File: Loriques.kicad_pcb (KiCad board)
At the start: 4 copper layers, 144.8 x 106.7 mm, 130 parts, among them IC10 MAX17263LETD+T, IC12 TPS22975, IC14 W25Q64FWSSIG, IC19 TPS22975, IC2 MCP73871, IC3 HDC2080, IC4 TPS2013A, IC5 CAT25160VI-GT3, IC6 SN74LVC244A, IC7 LP38691-ADJ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

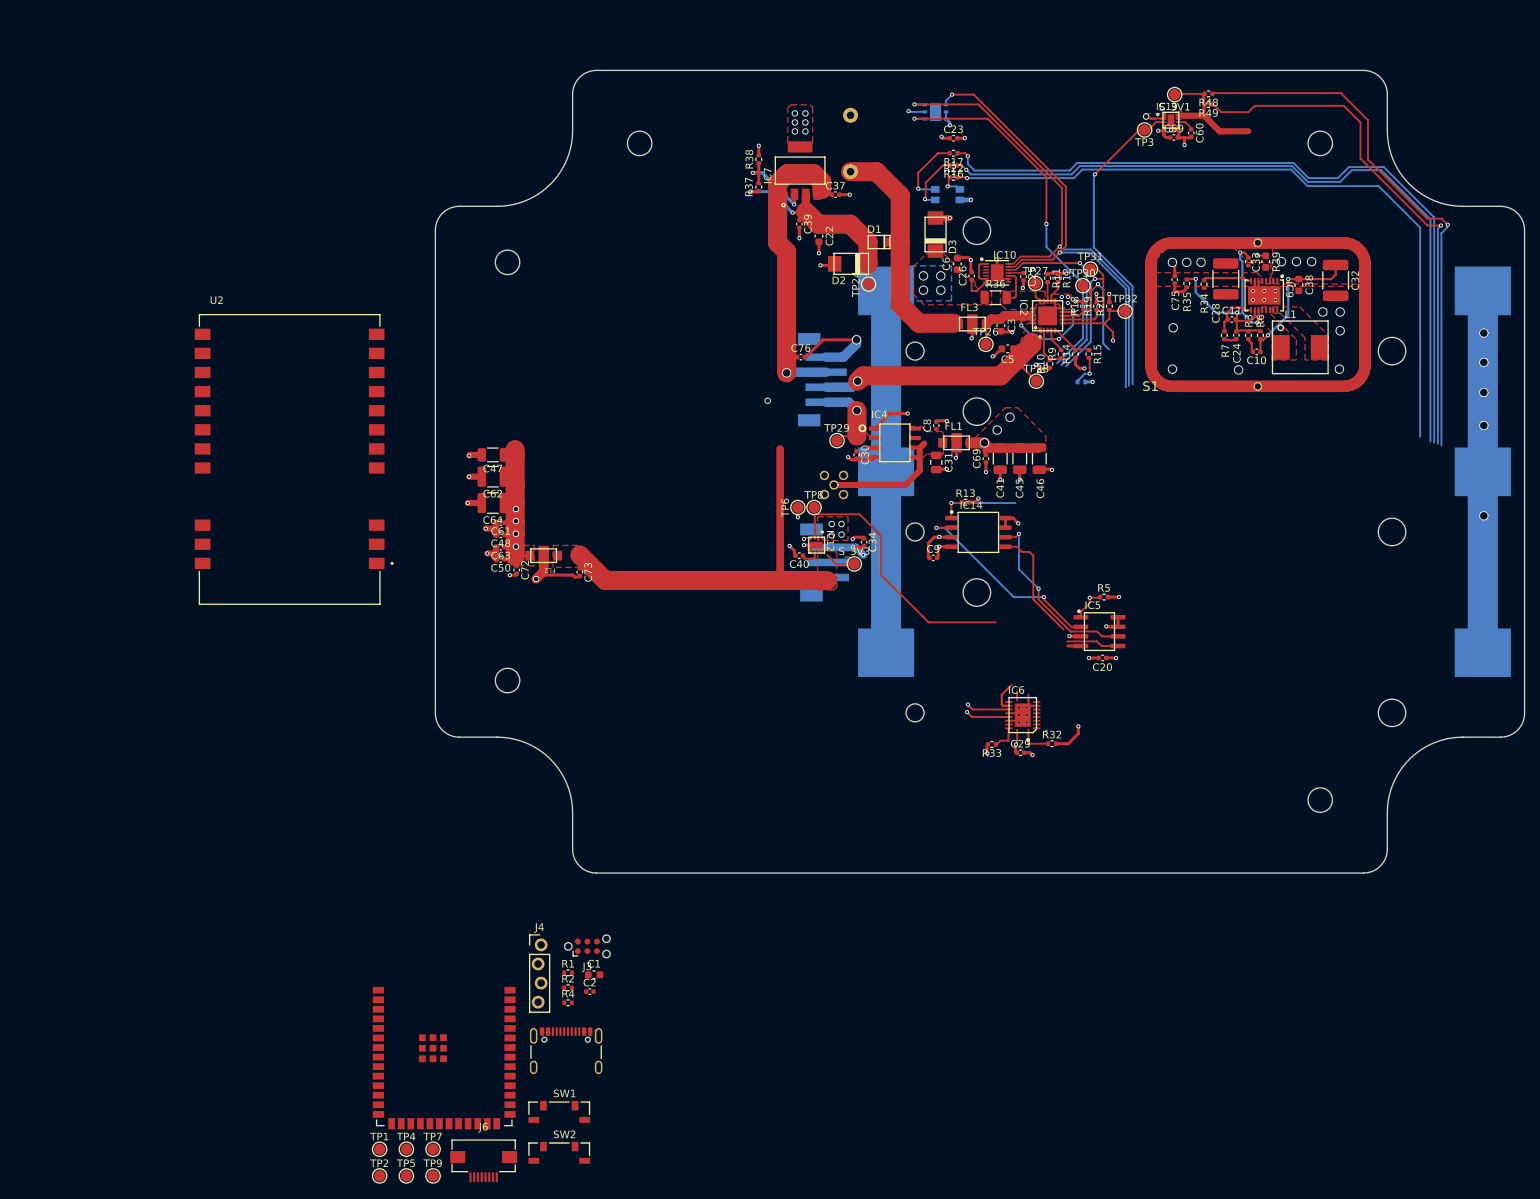
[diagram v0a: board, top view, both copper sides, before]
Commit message: name change to Loriques
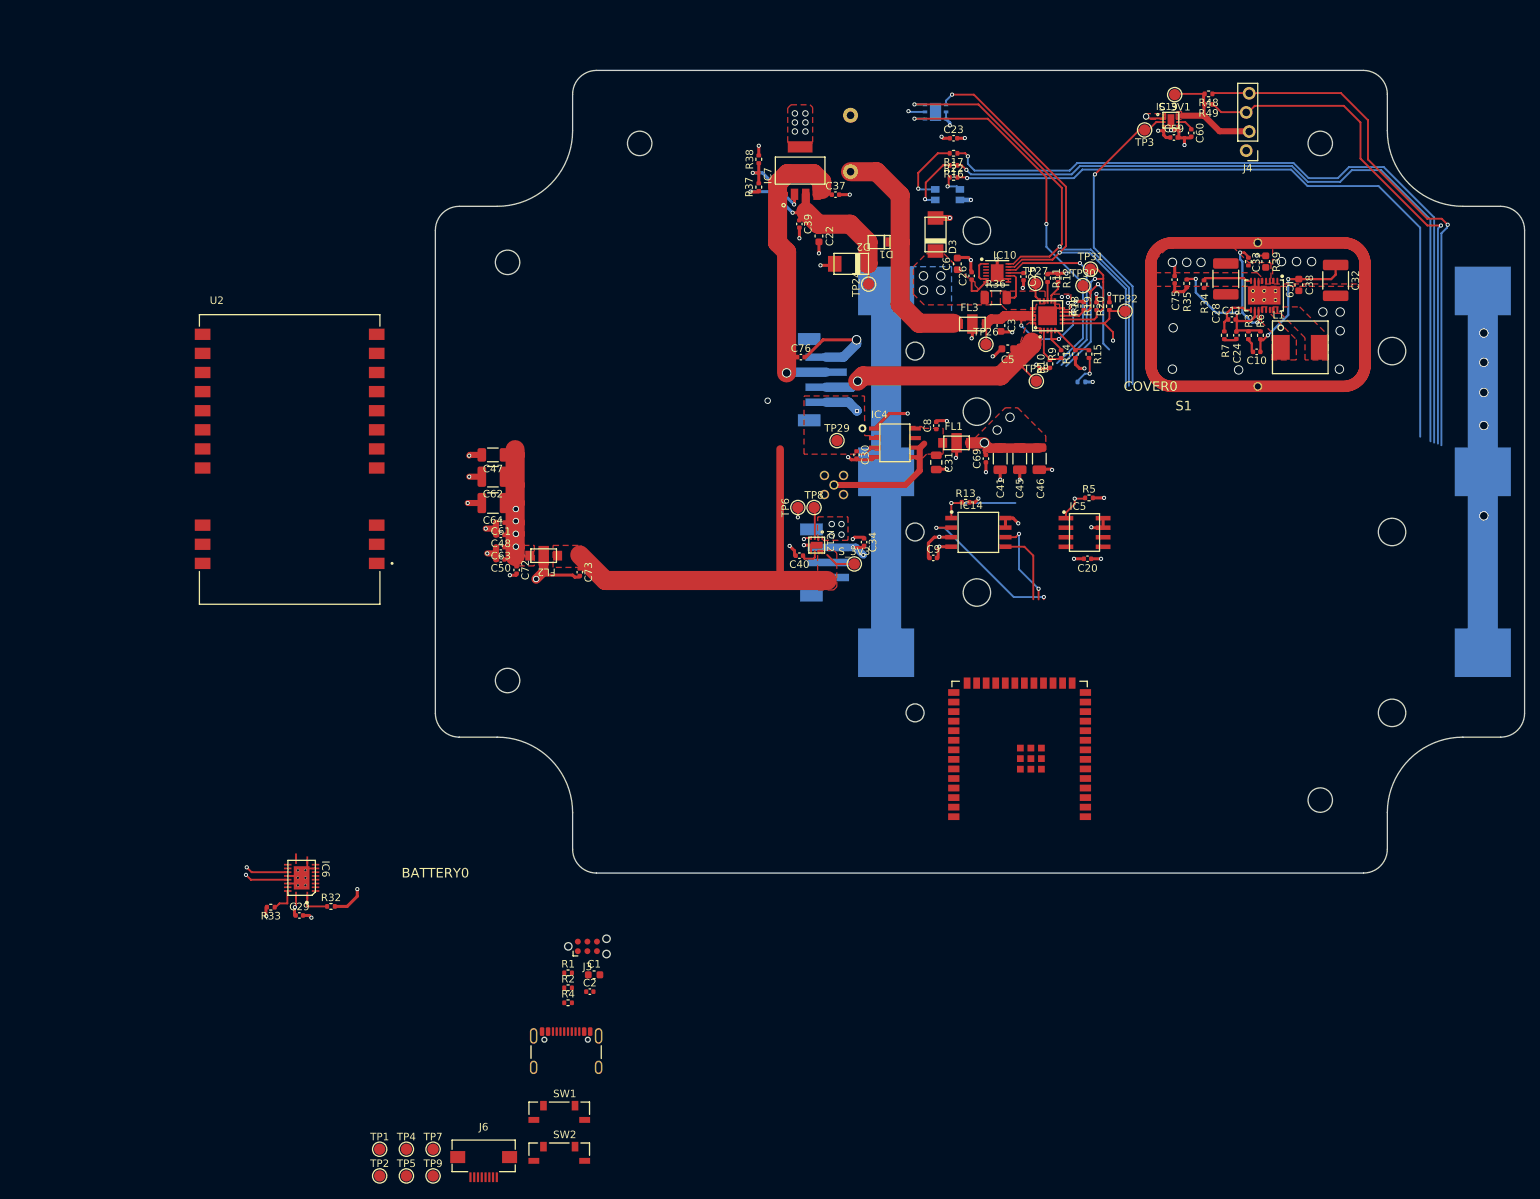
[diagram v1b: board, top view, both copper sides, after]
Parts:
- BATTERY0, COVER0: footprint autonode:NOTHING -> Loriques:NOTHING
- C27: footprint autonode:25PK4700MEFC16X25 -> Loriques:25PK4700MEFC16X25
- D1: footprint autonode:SOD−123FL -> Loriques:SOD−123FL
- D2, D3: footprint autonode:DO-214AC(SMA) -> Loriques:DO-214AC(SMA)
- FL1, FL2, FL3: footprint autonode:YFF31HC2A104MT000N -> Loriques:YFF31HC2A104MT000N
- IC10: footprint autonode:SON40P300X300X80-15T170X230N -> Loriques:SON40P300X300X80-15T170X230N
- IC12, IC19: footprint autonode:WSON8 -> Loriques:WSON8
- IC14: footprint autonode:SOIC127P790X216-8N -> Loriques:SOIC127P790X216-8N
- IC2: footprint autonode:QFN20-ML_4X4MM -> Loriques:QFN20-ML_4X4MM
- IC3: footprint autonode:DMB0006A -> Loriques:DMB0006A
- IC4: footprint autonode:R-PDSO-G8_NOPAD -> Loriques:R-PDSO-G8_NOPAD
- IC5: footprint autonode:SOIC127P600X175-8N -> Loriques:SOIC127P600X175-8N
- IC6: footprint autonode:R-PVQFN-N20 -> Loriques:R-PVQFN-N20
- IC7: footprint autonode:SOT-223-5 -> Loriques:SOT-223-5
- IC9: footprint autonode:SON50P400X500X80-17T244X434N -> Loriques:SON50P400X500X80-17T244X434N
- J1: footprint autonode:JST-PH-3-SMT -> Loriques:JST-PH-3-SMT
- J2: footprint autonode:JST-PH-4-SMT -> Loriques:JST-PH-4-SMT
- J4: footprint autonode:PinHeader_1x04_P2.54mm_Vertical_shifted -> Loriques:PinHeader_1x04_P2.54mm_Vertical_shifted
- J5: footprint autonode:MMCX-P-P-H-ST-TH1 -> Loriques:MMCX-P-P-H-ST-TH1
- J6: footprint autonode:FPC-SMD_P0.50-8P_FGS-XJ-H2.0 -> Loriques:FPC-SMD_P0.50-8P_FGS-XJ-H2.0
- J7: footprint autonode:USB_C_Receptacle_GCT_USB4105-xx-A -> Loriques:USB_C_Receptacle_GCT_USB4105-xx-A
- L1: footprint autonode:HCMA0703-2R2-R -> Loriques:HCMA0703-2R2-R
- LED0: footprint autonode:PLCC140P350X320X210-4 -> Loriques:PLCC140P350X320X210-4
- S1: footprint autonode:MS288-10F -> Loriques:MS288-10F
- SW1, SW2: footprint autonode:SW_TL3330AF130QG_EWI -> Loriques:SW_TL3330AF130QG_EWI
- U1: footprint autonode:ESP32-S3-WROOM-1 -> Loriques:ESP32-S3-WROOM-1
- U2: footprint autonode:E22-900M30S -> Loriques:E22-900M30S
- moved J4 141.5 mm to (184.1, 62.3), turned to 180 degrees
- moved C29 98.3 mm to (58.0, 164.0)
- moved IC6 98.3 mm to (58.3, 159.0)
- moved R32 98.3 mm to (62.2, 162.8)
- moved R33 98.3 mm to (54.2, 162.9)
- moved U1 86.1 mm to (153.8, 142.6), turned to 180 degrees
- moved C20 13.3 mm to (162.8, 116.6)
- moved IC5 13.3 mm to (162.4, 113.1)
- moved R5 13.3 mm to (163.0, 108.5)
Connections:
- J2 pad 1: /Power Input/VOUT -> GND
- J2 pad 2: /Power Input/VOUT_S1 -> /Power Input/PANEL_IN
- J2 pad 3: /Power Input/PANEL_IN -> /Power Input/VOUT_S1
- J2 pad 4: GND -> /Power Input/VOUT
- S_3V1 pad 1: (no net) -> /MCU/DISP_3V3
- S_3V3 pad 1: (no net) -> /Radio/RADIO_3V3
- TP24 pad 1: (no net) -> Net-(IC7-OUT)
- TP26 pad 1: (no net) -> /Power Input/CHARGE_IN
- TP27 pad 1: (no net) -> /Power Input/VBAT
- TP28 pad 1: (no net) -> /Power Input/VOUT_S1
- TP29 pad 1: (no net) -> /Power Input/VOUT
- TP3 pad 1: (no net) -> /MCU/DISP_EN
- TP30 pad 1: (no net) -> /MCU/STAT1
- TP31 pad 1: (no net) -> /MCU/STAT2
- TP32 pad 1: (no net) -> /MCU/PG
- TP6 pad 1: (no net) -> /MCU/3V3
- TP8 pad 1: (no net) -> /MCU/RADIO_EN
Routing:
- net /MCU/RADIO_EN: track 37.2 -> 4.09 mm
- net GND: track 195.4 -> 181.6 mm, vias 68 -> 67
- net /MCU/FLASH_MOSI: track 22.7 -> 9.99 mm
- net /MCU/FLASH_CLK: track 24.4 -> 11.8 mm
- net /MCU/FLASH_MISO: track 26.9 -> 20.4 mm
- net /Power Input/VOUT: track 0.00 -> 4.62 mm, vias 0 -> 1
- net /Radio/TXEN: track 4.18 -> 0.00 mm
- net /MCU/3V3: track 74.7 -> 73.2 mm
- net /Power Input/VBAT_IN: vias 0 -> 4
- net (no net): vias 8 -> 3
- added copper zone on F.Cu, net /Power Input/VBAT
- added copper zone on B.Cu, net /Power Input/VBAT_IN
- added copper zone on F.Cu, net /Power Input/VBAT_IN
- added copper zone on F.Cu, net /Power Input/VOUT
- added copper zone on F.Cu, net /Power Input/VOUT_LIMITED
- added copper zone on F.Cu, net /Power Input/VOUT_S1
- added copper zone on F.Cu, net /Voltage Regulator/SW1
- added copper zone on F.Cu, net /Voltage Regulator/SW2
- removed copper zone on B.Cu, net (none)

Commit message: added lots of 3d models
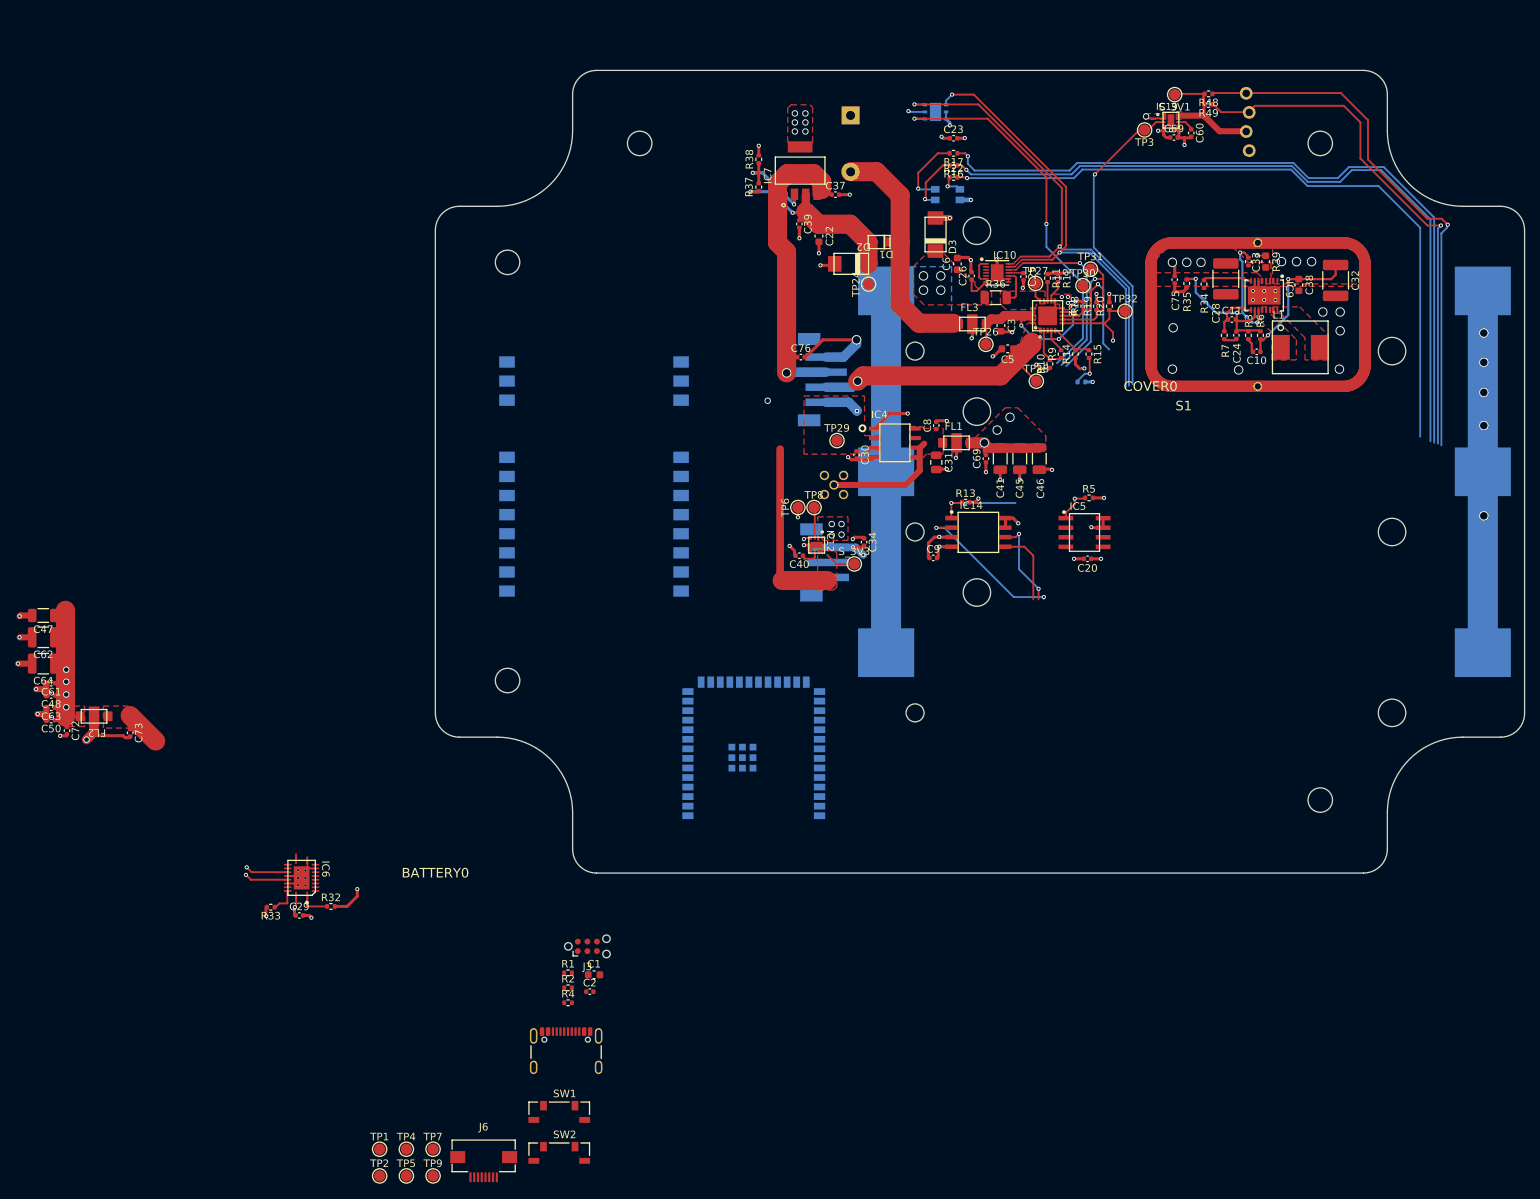
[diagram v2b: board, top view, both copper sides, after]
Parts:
- added G***: LOGO, Loriques:loriques_logo, B.Cu at (166.5, 149.7)
- B1, B2, B3: footprint autonode:1042 -> Loriques:1042
- C27: footprint Loriques:25PK4700MEFC16X25 -> Capacitor_THT:CP_Radial_D16.0mm_P7.50mm
- J4, U1, U2: moved to B.Cu
- moved C47 63.5 mm to (24.0, 124.1)
- moved C62 63.5 mm to (24.0, 127.0)
- moved C64 63.5 mm to (24.0, 130.5)
- moved C73 63.5 mm to (35.5, 139.7)
- moved FL2 63.5 mm to (30.7, 137.5)
- moved C48 63.5 mm to (25.0, 134.8)
- moved C50 63.5 mm to (25.0, 138.0)
- moved C61 63.5 mm to (25.0, 133.1)
- moved C63 63.5 mm to (25.0, 136.4)
- moved C72 63.5 mm to (27.1, 139.4)
- moved U2 40.5 mm to (97.2, 104.2)
- moved U1 35.4 mm to (118.4, 142.5), turned to 0 degrees
- moved C27 3.74 mm to (131.3, 57.6), turned to -90 degrees
- turned J4 to 0 degrees
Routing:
- net /Radio/RADIO_3V3: track 56.5 -> 33.0 mm
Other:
- board text added: "REV A"
